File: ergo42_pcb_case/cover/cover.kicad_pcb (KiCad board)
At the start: 2 copper layers, 80.9 x 24.8 mm, 5 parts

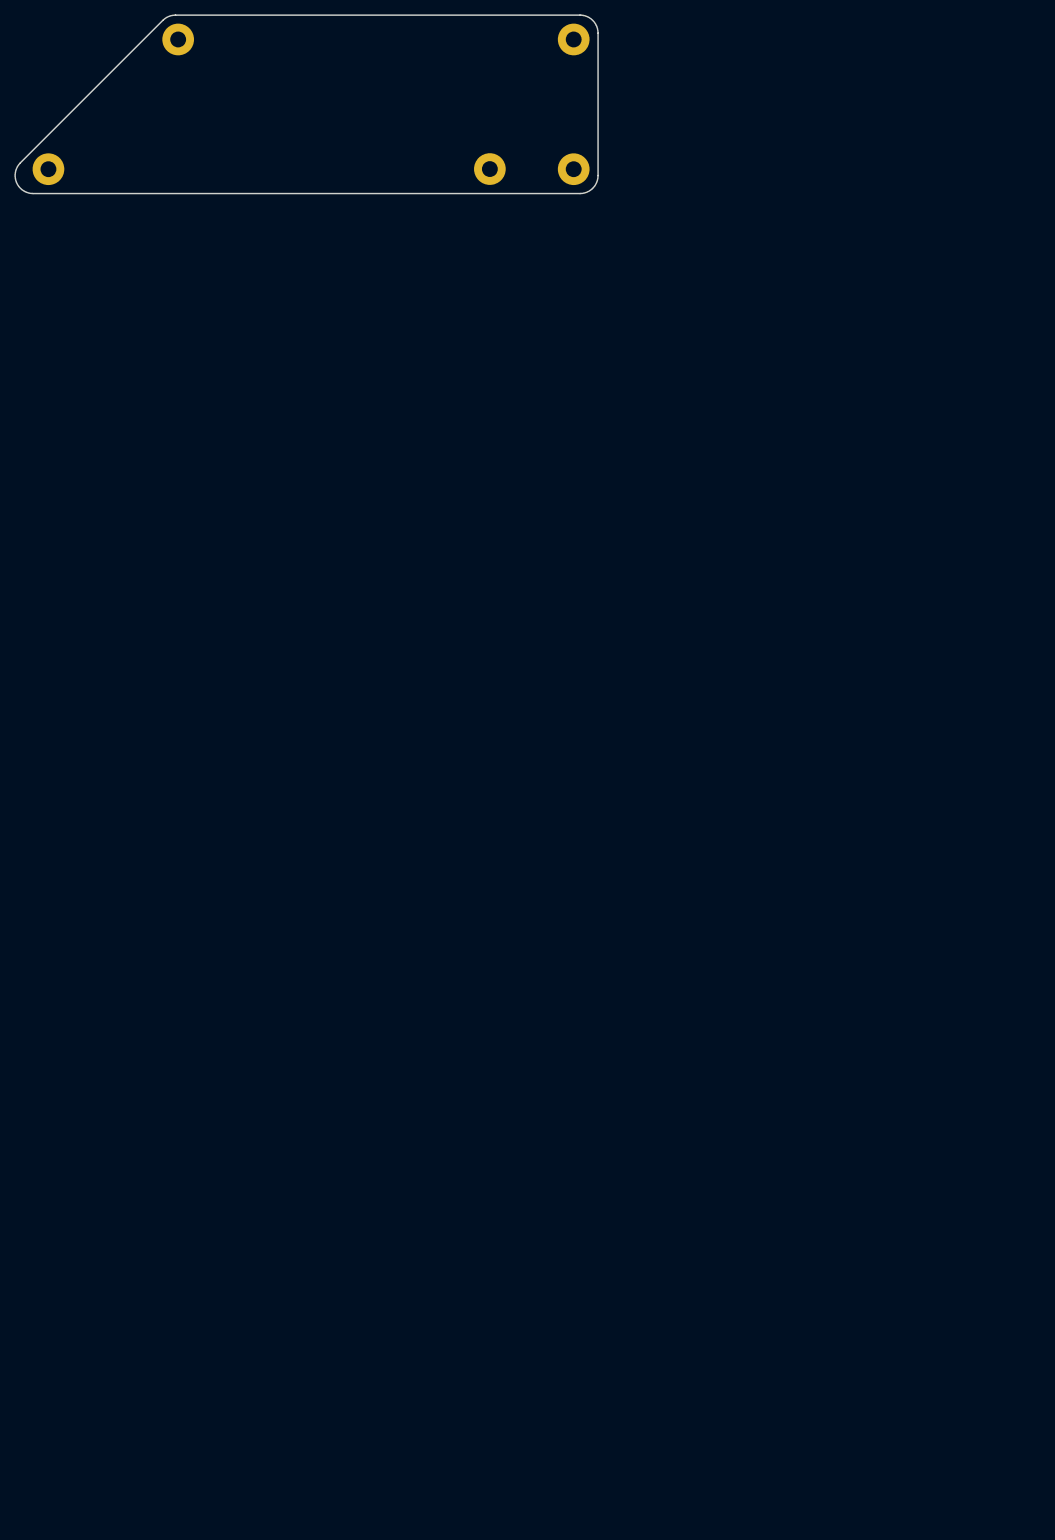
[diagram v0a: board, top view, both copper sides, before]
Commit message: Reimport DXFs into middle of the page
PDF plotter has hard times with anything outside A4 page...
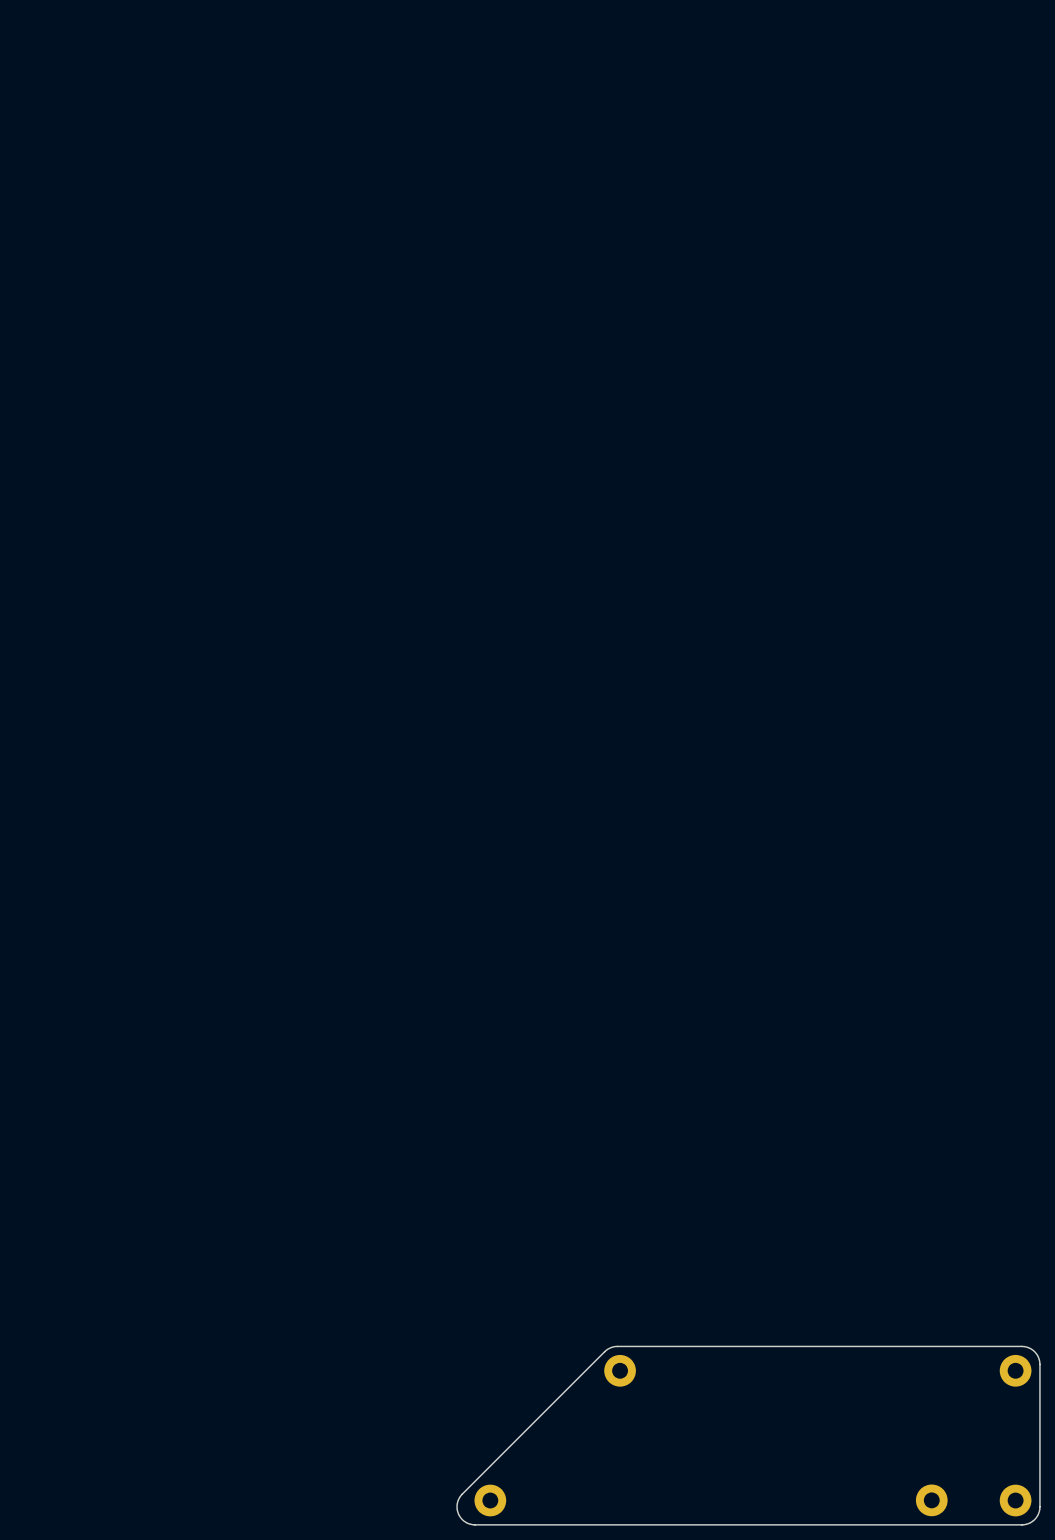
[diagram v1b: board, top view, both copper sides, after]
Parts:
- removed the REF** at (111.8, -73.0)
- removed the REF** at (123.4, -91.0)
- removed the REF** at (123.4, -73.0)
- removed the REF** at (50.5, -73.0)
- removed the REF** at (68.5, -91.0)
- added REF**: MountingHole_2.2mm_M2_Pad, MountingHole_2.2mm_M2_Pad, F.Cu at (184.7, 111.8)
- added REF**: MountingHole_2.2mm_M2_Pad, MountingHole_2.2mm_M2_Pad, F.Cu at (111.8, 111.8)
- added REF**: MountingHole_2.2mm_M2_Pad, MountingHole_2.2mm_M2_Pad, F.Cu at (173.1, 111.8)
- added REF**: MountingHole_2.2mm_M2_Pad, MountingHole_2.2mm_M2_Pad, F.Cu at (184.7, 93.8)
- added REF**: MountingHole_2.2mm_M2_Pad, MountingHole_2.2mm_M2_Pad, F.Cu at (129.8, 93.8)
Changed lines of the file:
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@@
   )
   (module MountingHole_2.2mm_M2_Pad (layer F.Cu)
-    (at 111.76 -73.025)
+    (at 184.73 111.78)
     (descr "Mounting Hole 2.2mm, M2")
     (tags "mounting hole 2.2mm m2")
@@
   )
   (module MountingHole_2.2mm_M2_Pad (layer F.Cu)
-    (at 123.395 -91.01)
+    (at 111.824507 111.78)
     (descr "Mounting Hole 2.2mm, M2")
     (tags "mounting hole 2.2mm m2")
@@
   )
   (module MountingHole_2.2mm_M2_Pad (layer F.Cu)
-    (at 123.395 -73.005)
+    (at 173.095 111.76)
     (descr "Mounting Hole 2.2mm, M2")
     (tags "mounting hole 2.2mm m2")
@@
   )
   (module MountingHole_2.2mm_M2_Pad (layer F.Cu)
-    (at 50.489507 -73.005)
+    (at 184.73 93.775)
     (descr "Mounting Hole 2.2mm, M2")
     (tags "mounting hole 2.2mm m2")
@@
   )
   (module MountingHole_2.2mm_M2_Pad (layer F.Cu)
-    (at 68.494507 -91.01)
+    (at 129.829507 93.775)
     (descr "Mounting Hole 2.2mm, M2")
     (tags "mounting hole 2.2mm m2")
@@
     (pad 1 thru_hole circle (at 0 0) (size 4.4 4.4) (drill 2.2) (layers *.Cu *.Mask))
   )
-  (gr_circle (center 68.494507 -91.01) (end 69.669507 -91.01) (layer Eco1.User) (width 0.2))
-  (gr_circle (center 50.489507 -73.005) (end 51.664507 -73.005) (layer Eco1.User) (width 0.2))
-  (gr_circle (center 123.395 -73.005) (end 124.57 -73.005) (layer Eco1.User) (width 0.2))
-  (gr_circle (center 123.395 -91.01) (end 124.57 -91.01) (layer Eco1.User) (width 0.2))
-  (gr_circle (center 111.76 -73.025) (end 112.935 -73.025) (layer Eco1.User) (width 0.2))
-  (gr_arc (start 48.364999 -72.125) (end 46.597233 -73.892766) (angle -135) (layer Edge.Cuts) (width 0.2))
-  (gr_line (start 124.274999 -69.625) (end 48.364999 -69.625) (layer Edge.Cuts) (width 0.2))
-  (gr_arc (start 124.274999 -72.125) (end 124.274999 -69.625) (angle -90) (layer Edge.Cuts) (width 0.2))
-  (gr_line (start 126.774999 -91.889999) (end 126.774999 -72.125) (layer Edge.Cuts) (width 0.2))
-  (gr_arc (start 124.274999 -91.889999) (end 126.774999 -91.889999) (angle -90) (layer Edge.Cuts) (width 0.2))
-  (gr_line (start 68.129999 -94.39) (end 124.274999 -94.389999) (layer Edge.Cuts) (width 0.2))
-  (gr_arc (start 68.129999 -91.89) (end 68.129999 -94.39) (angle -45) (layer Edge.Cuts) (width 0.2))
-  (gr_line (start 46.597233 -73.892766) (end 66.362233 -93.657766) (layer Edge.Cuts) (width 0.2))
+  (gr_line (start 188.109999 92.895001) (end 188.109999 112.66) (layer Edge.Cuts) (width 0.2))
+  (gr_line (start 107.932233 110.892234) (end 127.697233 91.127234) (layer Edge.Cuts) (width 0.2))
+  (gr_arc (start 185.609999 112.66) (end 185.609999 115.16) (angle -90) (layer Edge.Cuts) (width 0.2))
+  (gr_circle (center 129.829507 93.775) (end 131.004507 93.775) (layer Eco1.User) (width 0.2))
+  (gr_circle (center 184.73 93.775) (end 185.905 93.775) (layer Eco1.User) (width 0.2))
+  (gr_arc (start 185.609999 92.895001) (end 188.109999 92.895001) (angle -90) (layer Edge.Cuts) (width 0.2))
+  (gr_arc (start 109.7 112.66) (end 107.932233 110.892234) (angle -135) (layer Edge.Cuts) (width 0.2))
+  (gr_line (start 129.465 90.395) (end 185.609999 90.395001) (layer Edge.Cuts) (width 0.2))
+  (gr_arc (start 129.465 92.895) (end 129.465 90.395) (angle -45) (layer Edge.Cuts) (width 0.2))
+  (gr_line (start 185.609999 115.16) (end 109.7 115.16) (layer Edge.Cuts) (width 0.2))
+  (gr_circle (center 173.095 111.76) (end 174.27 111.76) (layer Eco1.User) (width 0.2))
+  (gr_circle (center 111.824507 111.78) (end 112.999507 111.78) (layer Eco1.User) (width 0.2))
+  (gr_circle (center 184.73 111.78) (end 185.905 111.78) (layer Eco1.User) (width 0.2))
 )
